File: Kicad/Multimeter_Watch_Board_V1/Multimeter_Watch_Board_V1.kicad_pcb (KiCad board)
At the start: 4 copper layers, 55 x 46 mm, 38 parts, among them J1 AudioJack3_Ground_renamedPins, J2 AudioJack3_Ground_renamedPins, J3 AudioJack3_Ground_renamedPins, J4 Conn_01x16_Female, J5 Conn_01x16_Female, U1 PCF85163-SO08, U2 AD8592, Y1 32kHz

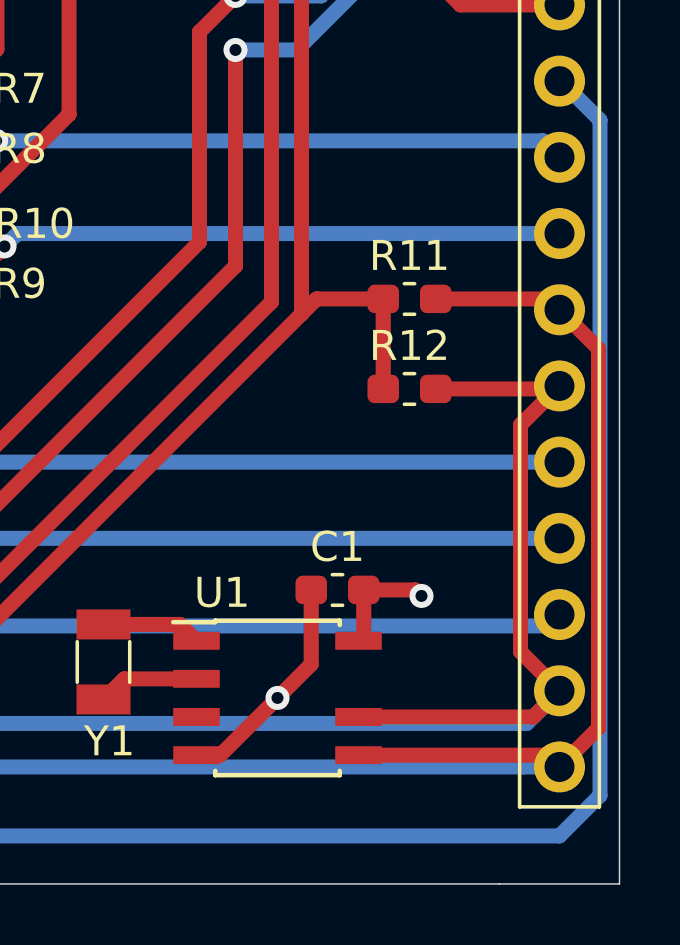
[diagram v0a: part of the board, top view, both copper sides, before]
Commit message: fix switched I2C pins
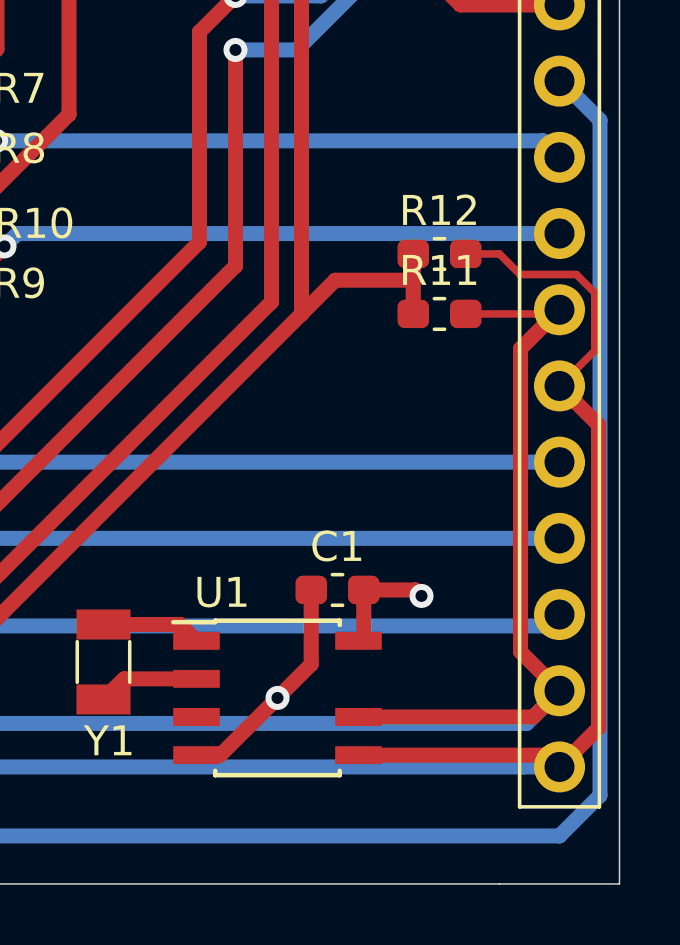
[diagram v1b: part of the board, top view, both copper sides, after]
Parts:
- moved R12 4.61 mm to (149.0, 75.0)
- moved R11 1.12 mm to (149.0, 77.0)
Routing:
- net /SCL: track 72.3 -> 74.4 mm
- net /SDA: track 78.7 -> 80.4 mm

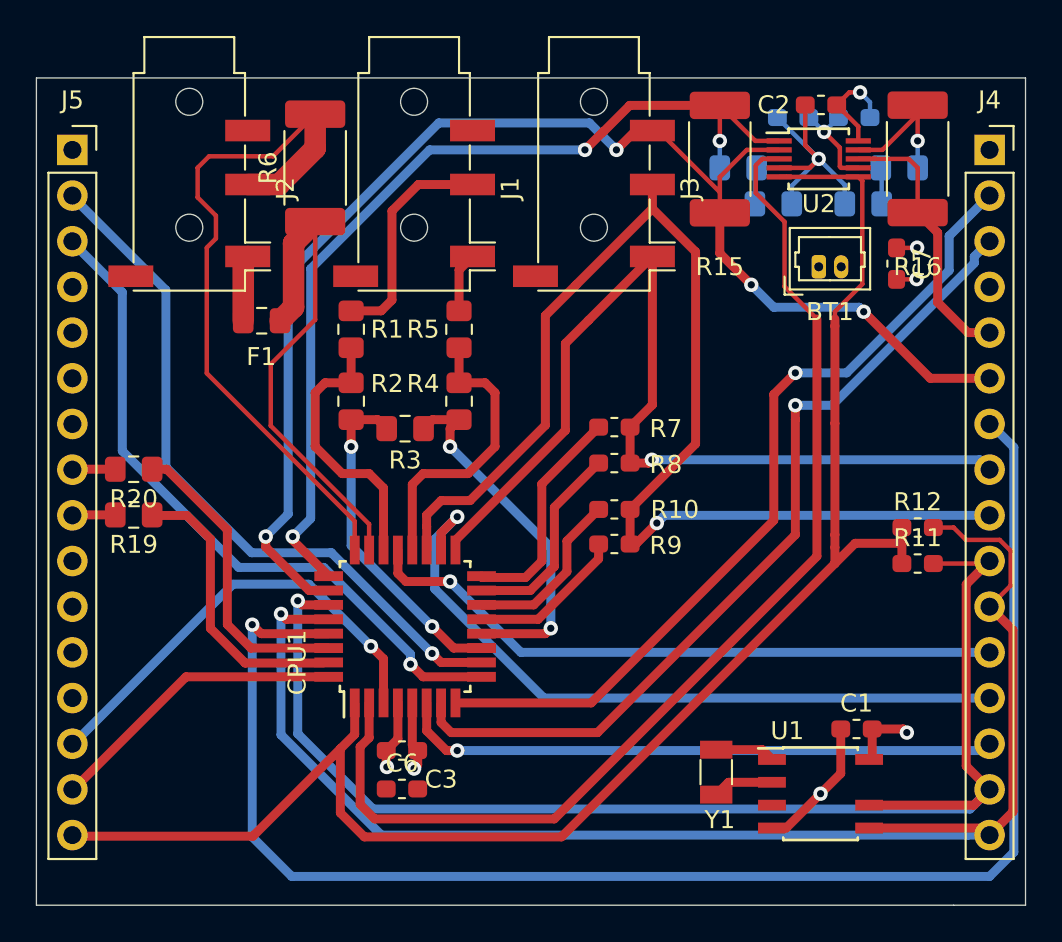
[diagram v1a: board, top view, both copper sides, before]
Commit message: actually add logos from last commit
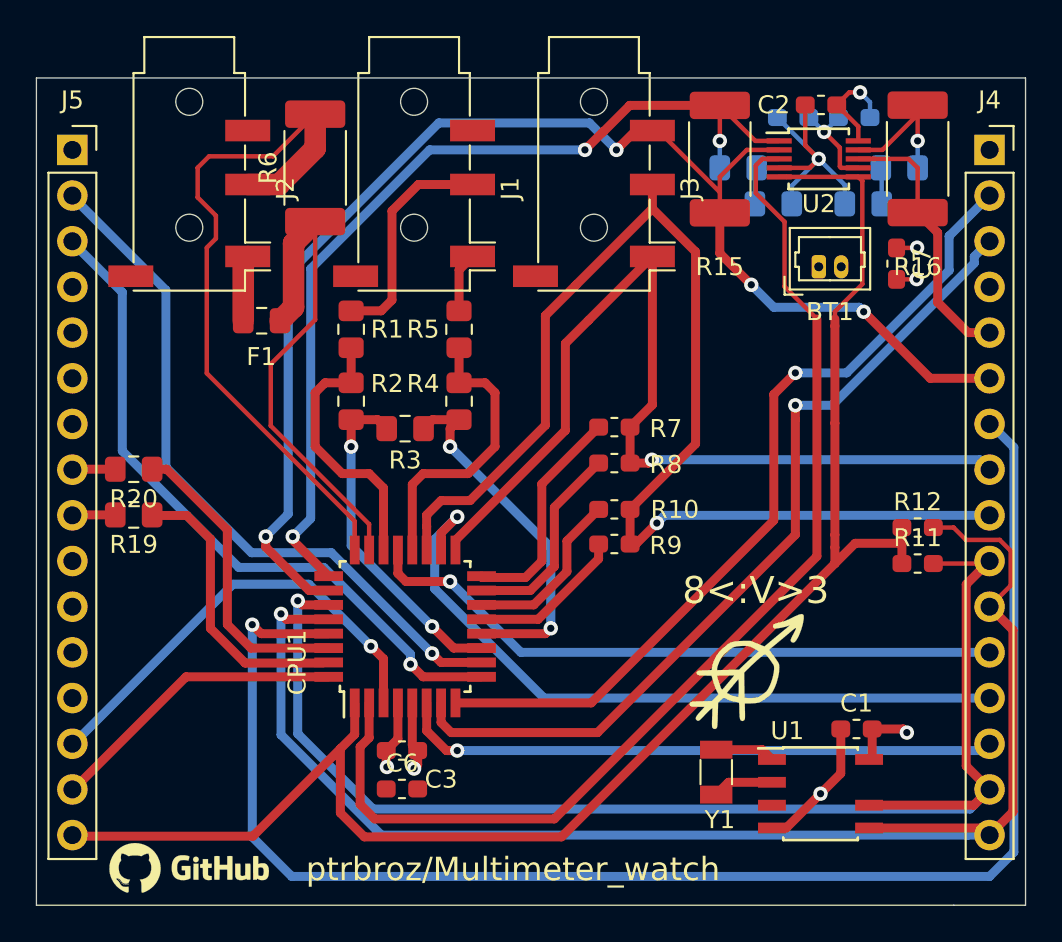
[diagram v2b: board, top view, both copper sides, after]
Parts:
- added G***: LOGO, Multimeter_Watch_Custom_Footprints:nouth_signature, F.Cu at (139.5, 83.0)
- added G***: LOGO, Multimeter_Watch_Custom_Footprints:github_logo, F.Cu at (108.5, 94.0)
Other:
- board text added: "8<:V>3"
- board text added: "ptrbroz/Multimeter_watch"

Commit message: ground plane around crystal, silkscreen adjustments
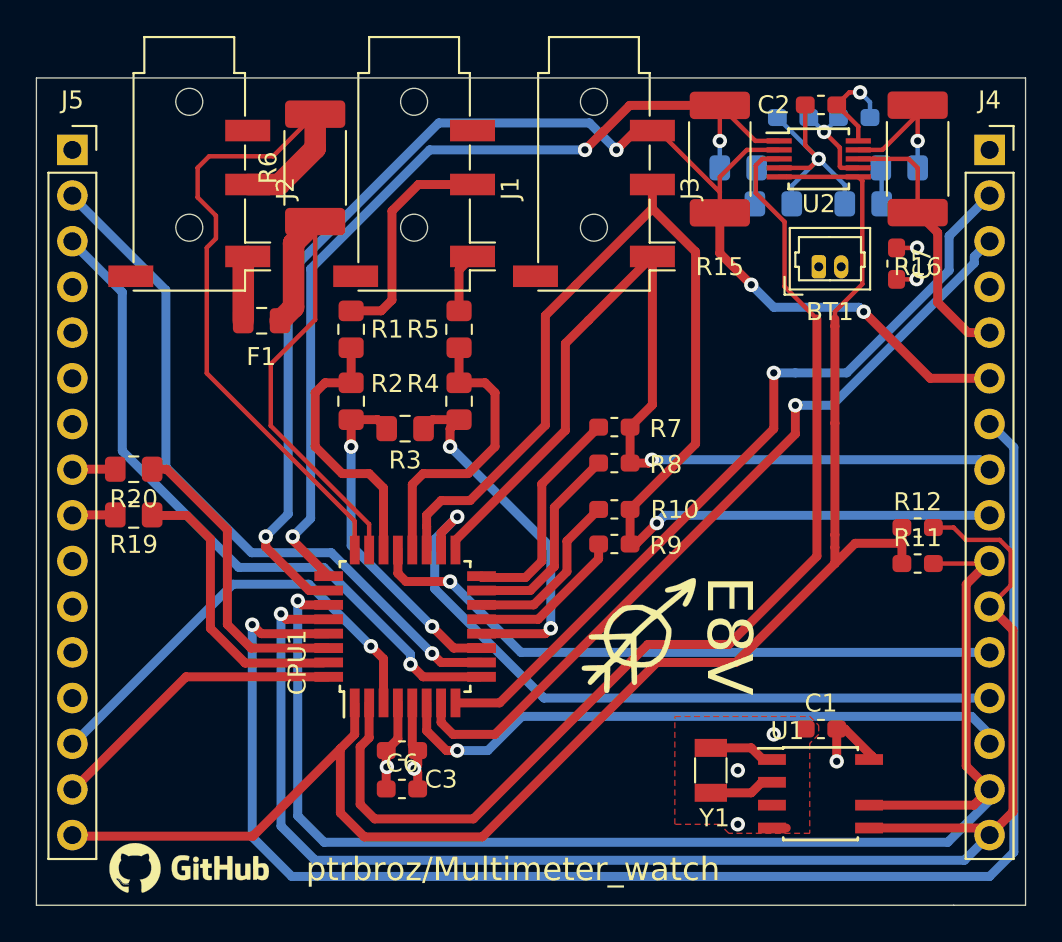
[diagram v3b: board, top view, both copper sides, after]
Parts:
- moved G*** 6.32 mm to (133.5, 81.0)
- moved C1 1.97 mm to (143.6, 86.2)
- moved Y1 0.32 mm to (137.5, 88.5)
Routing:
- net /GND: track 27.7 -> 22.2 mm, vias 4 -> 6
- net /SCL: track 74.4 -> 79.0 mm
- net /SDA: track 80.4 -> 84.6 mm
- net /PB6: track 48.1 -> 44.9 mm
- net /PB7: track 47.2 -> 44.9 mm
- net /VCC: track 14.7 -> 16.8 mm
- net /PE5: track 33.5 -> 35.6 mm
- added copper zone on F.Cu, net /GND
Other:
- board text added: "ADC11"
- board text added: "ADC3"
- board text added: "ADC6"
- board text added: "D0"
- board text added: "D1"
- board text added: "E8V"
- board text added: "GND"
- board text added: "PB6"
- board text added: "PB7"
- board text added: "PD2"
- board text added: "PD3"
- board text added: "PD5"
- board text added: "PD6"
- board text added: "PE4"
- board text added: "PE5"
- board text added: "RESET"
- board text added: "SCL"
- board text added: "SDA"
- board text added: "SWC"
- board text added: "SWD"
- board text added: "VCC"
- board text added: "VCC/2"
- board text removed: "8<:V>3"

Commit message: reset pullup
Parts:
- added R21: R, Resistor_SMD:R_0603_1608Metric_Pad1.05x0.95mm_HandSolder, F.Cu at (112.0, 77.9)
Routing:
- net /VCC: track 16.8 -> 20.0 mm, vias 4 -> 5
- net /RESET: track 84.4 -> 86.1 mm

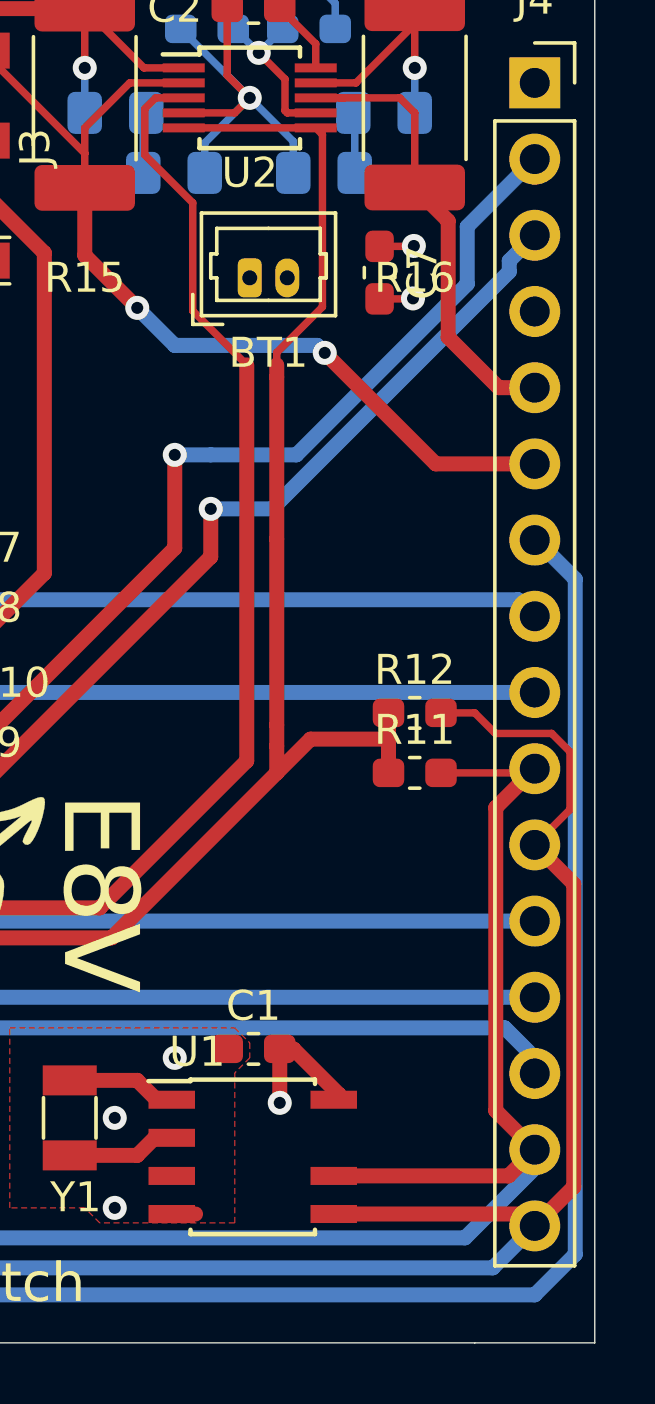
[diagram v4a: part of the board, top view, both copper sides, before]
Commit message: group rlc tester pins on right header
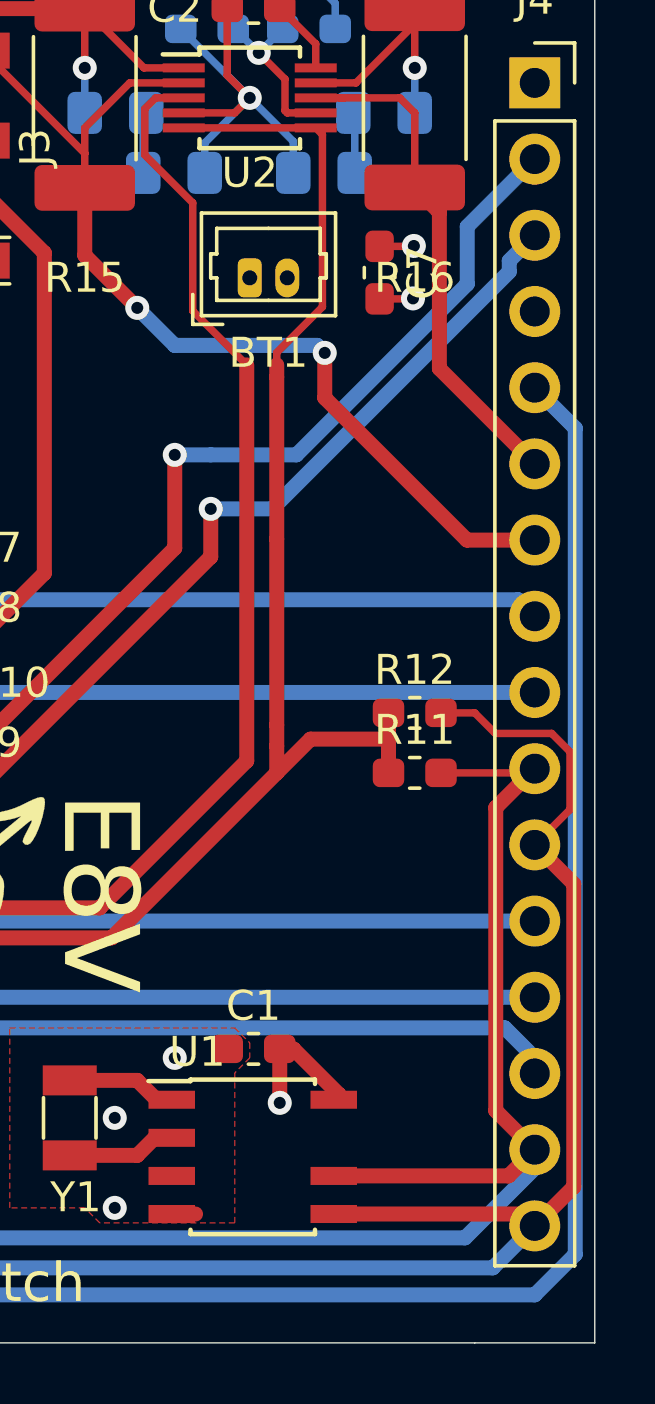
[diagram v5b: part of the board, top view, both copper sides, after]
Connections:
- J4 pad 5: /VCC_HALF -> /RESET
- J4 pad 6: /ADC3 -> /VCC_HALF
- J4 pad 7: /RESET -> /ADC3
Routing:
- net /RESET: track 86.1 -> 91.2 mm
- net /ADC3: track 76.2 -> 78.2 mm
- net /VCC_HALF: track 15.8 -> 17.7 mm
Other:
- board text added: "DAC OUT"
- board text removed: "ADC3"
